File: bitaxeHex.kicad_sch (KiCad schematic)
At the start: 26 parts, among them J1 Screw Terminal, J2 Screw Terminal

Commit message: adjust new mounting hole locations
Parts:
- H10, H13, H14, H15, H5, H6, H7, H8, H9: footprint bitaxe:2.2mm_mounting -> bitaxe:3.1mm_mounting
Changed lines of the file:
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@@
       (effects (font (size 1.27 1.27)) (justify left))
     )
-    (property "Footprint" "bitaxe:2.2mm_mounting" (at 119.38 147.955 0)
+    (property "Footprint" "bitaxe:3.1mm_mounting" (at 119.38 147.955 0)
       (effects (font (size 1.27 1.27)) hide)
     )
@@
       (effects (font (size 1.27 1.27)) (justify left))
     )
-    (property "Footprint" "bitaxe:2.2mm_mounting" (at 119.38 193.675 0)
+    (property "Footprint" "bitaxe:3.1mm_mounting" (at 119.38 193.675 0)
       (effects (font (size 1.27 1.27)) hide)
     )
@@
       (effects (font (size 1.27 1.27)) (justify left))
     )
-    (property "Footprint" "bitaxe:2.2mm_mounting" (at 119.38 180.34 0)
+    (property "Footprint" "bitaxe:3.1mm_mounting" (at 119.38 180.34 0)
       (effects (font (size 1.27 1.27)) hide)
     )
@@
       (effects (font (size 1.27 1.27)) (justify left))
     )
-    (property "Footprint" "bitaxe:2.2mm_mounting" (at 119.38 154.305 0)
+    (property "Footprint" "bitaxe:3.1mm_mounting" (at 119.38 154.305 0)
       (effects (font (size 1.27 1.27)) hide)
     )
@@
       (effects (font (size 1.27 1.27)) (justify left))
     )
-    (property "Footprint" "bitaxe:2.2mm_mounting" (at 119.38 141.605 0)
+    (property "Footprint" "bitaxe:3.1mm_mounting" (at 119.38 141.605 0)
       (effects (font (size 1.27 1.27)) hide)
     )
@@
       (effects (font (size 1.27 1.27)) (justify left))
     )
-    (property "Footprint" "bitaxe:2.2mm_mounting" (at 119.38 160.655 0)
+    (property "Footprint" "bitaxe:3.1mm_mounting" (at 119.38 160.655 0)
       (effects (font (size 1.27 1.27)) hide)
     )
@@
       (effects (font (size 1.27 1.27)) (justify left))
     )
-    (property "Footprint" "bitaxe:2.2mm_mounting" (at 119.38 187.325 0)
+    (property "Footprint" "bitaxe:3.1mm_mounting" (at 119.38 187.325 0)
       (effects (font (size 1.27 1.27)) hide)
     )
@@
       (effects (font (size 1.27 1.27)) (justify left))
     )
-    (property "Footprint" "bitaxe:2.2mm_mounting" (at 119.38 173.99 0)
+    (property "Footprint" "bitaxe:3.1mm_mounting" (at 119.38 173.99 0)
       (effects (font (size 1.27 1.27)) hide)
     )
@@
       (effects (font (size 1.27 1.27)) (justify left))
     )
-    (property "Footprint" "bitaxe:2.2mm_mounting" (at 119.38 167.64 0)
-      (effects (font (size 1.27 1.27)) hide)
-    )
+    (property "Footprint" "bitaxe:3.1mm_mounting" (at 119.38 167.64 0)
+      (effects (font (size 1.27 1.27)) hide)
+    )

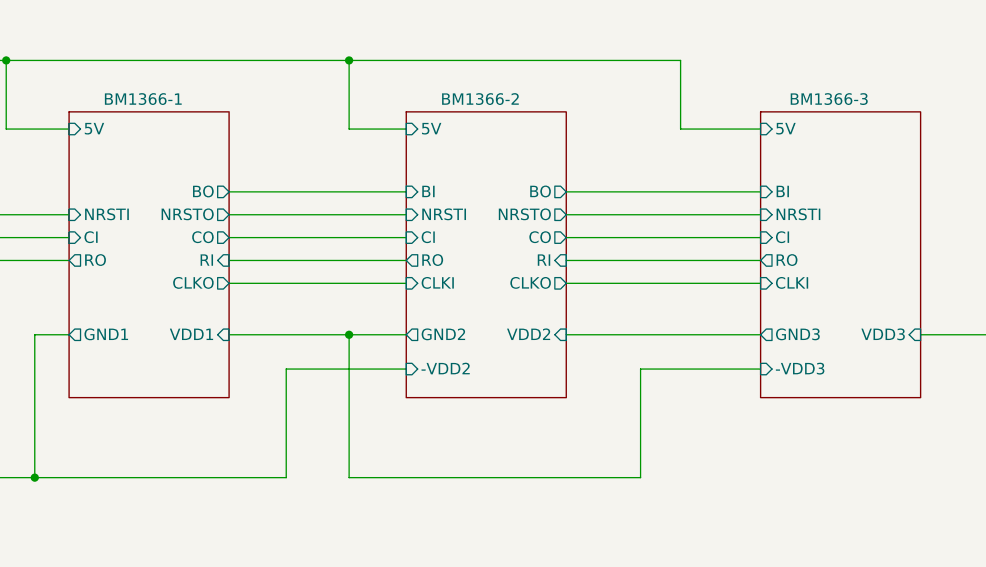
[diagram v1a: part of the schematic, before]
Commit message: remove 33R series resistors and other components, add mounting holes
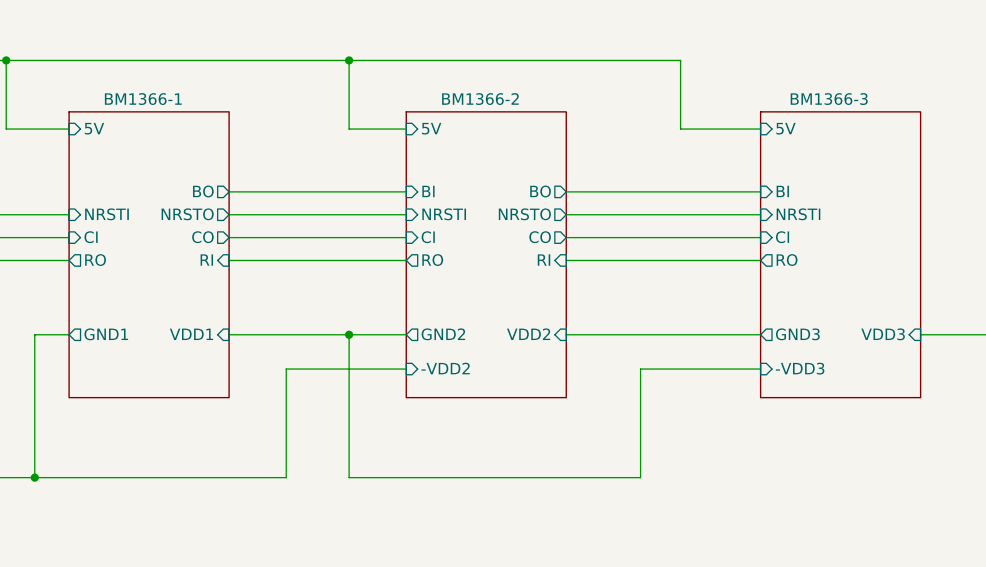
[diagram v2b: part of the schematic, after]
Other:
- sheet BM1366-1 ports: added none; removed CLKO
- sheet BM1366-2 ports: added none; removed CLKI, CLKO
- sheet BM1366-3 ports: added none; removed CLKI
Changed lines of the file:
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@@
   (title_block
     (title "bitaxeHex")
-    (date "2023-12-28")
-    (rev "302")
+    (date "2024-03-09")
+    (rev "303")
   )
   (junction (at 90.805 80.01) (diameter 0) (color 0 0 0 0)
@@
     (stroke (width 0) (type default))
   )
-  (wire (pts (xy 141.605 93.345) (xy 161.29 93.345))
-    (stroke (width 0) (type default))
-  )
   (wire (pts (xy 87.63 95.25) (xy 81.28 95.25))
     (stroke (width 0) (type default))
@@
   )
   (wire (pts (xy 37.465 40.64) (xy 45.72 40.64))
-    (stroke (width 0) (type default))
-  )
-  (wire (pts (xy 179.07 93.345) (xy 200.66 93.345))
     (stroke (width 0) (type default))
   )
@@
       (effects (font (size 1.27 1.27)) (justify right))
     )
-    (pin "CLKO" output (at 141.605 93.345 0)
-      (effects (font (size 1.27 1.27)) (justify right))
-    )
     (pin "CI" input (at 123.825 88.265 180)
       (effects (font (size 1.27 1.27)) (justify left))
@@
       (effects (font (size 1.27 1.27)) (justify left))
     )
-    (pin "CLKI" input (at 161.29 93.345 180)
-      (effects (font (size 1.27 1.27)) (justify left))
-    )
     (pin "CI" input (at 161.29 88.265 180)
       (effects (font (size 1.27 1.27)) (justify left))
@@
     )
     (pin "VDD2" input (at 179.07 99.06 0)
-      (effects (font (size 1.27 1.27)) (justify right))
-    )
-    (pin "CLKO" output (at 179.07 93.345 0)
       (effects (font (size 1.27 1.27)) (justify right))
     )
@@
       (effects (font (size 1.27 1.27)) (justify left))
     )
-    (pin "CLKI" input (at 200.66 93.345 180)
-      (effects (font (size 1.27 1.27)) (justify left))
-    )

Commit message: generate BOM and gerber files for v303
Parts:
- H1, H2, H3, H4: now left out of the parts list
- renumbered H8 to H10, H9 to H11, H10 to H12, H11 to H5, H12 to H6, H5 to H7, H6 to H8, H7 to H9
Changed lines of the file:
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@@
 		(unit 1)
 		(exclude_from_sim no)
-		(in_bom yes)
+		(in_bom no)
 		(on_board yes)
 		(dnp no)
@@
 		(unit 1)
 		(exclude_from_sim no)
-		(in_bom yes)
+		(in_bom no)
 		(on_board yes)
 		(dnp no)
@@
 		(unit 1)
 		(exclude_from_sim no)
-		(in_bom yes)
+		(in_bom no)
 		(on_board yes)
 		(dnp no)
@@
 		(unit 1)
 		(exclude_from_sim no)
-		(in_bom yes)
+		(in_bom no)
 		(on_board yes)
 		(dnp no)
@@
 		(dnp no)
 		(fields_autoplaced yes)
-		(property "Reference" "H6"
+		(property "Reference" "H8"
 			(at 121.92 146.6849 0)
 			(effects
@@
 			(project "bitaxeHex"
 				(path "/e63e39d7-6ac0-4ffd-8aa3-1841a4541b55"
-					(reference "H6")
+					(reference "H8")
 					(unit 1)
 				)
@@
 		(dnp no)
 		(fields_autoplaced yes)
-		(property "Reference" "H11"
+		(property "Reference" "H5"
 			(at 88.265 180.34 90)
 			(effects
@@
 			(project "bitaxeHex"
 				(path "/e63e39d7-6ac0-4ffd-8aa3-1841a4541b55"
-					(reference "H11")
+					(reference "H5")
 					(unit 1)
 				)
@@
 		(dnp no)
 		(fields_autoplaced yes)
-		(property "Reference" "H12"
+		(property "Reference" "H6"
 			(at 88.265 187.325 90)
 			(effects
@@
 			(project "bitaxeHex"
 				(path "/e63e39d7-6ac0-4ffd-8aa3-1841a4541b55"
-					(reference "H12")
+					(reference "H6")
 					(unit 1)
 				)
@@
 		(dnp no)
 		(fields_autoplaced yes)
-		(property "Reference" "H7"
+		(property "Reference" "H9"
 			(at 121.92 153.0349 0)
 			(effects
@@
 			(project "bitaxeHex"
 				(path "/e63e39d7-6ac0-4ffd-8aa3-1841a4541b55"
-					(reference "H7")
+					(reference "H9")
 					(unit 1)
 				)
@@
 		(dnp no)
 		(fields_autoplaced yes)
-		(property "Reference" "H5"
+		(property "Reference" "H7"
 			(at 121.92 140.3349 0)
 			(effects
@@
 			(project "bitaxeHex"
 				(path "/e63e39d7-6ac0-4ffd-8aa3-1841a4541b55"
-					(reference "H5")
+					(reference "H7")
 					(unit 1)
 				)
@@
 		(dnp no)
 		(fields_autoplaced yes)
-		(property "Reference" "H8"
+		(property "Reference" "H10"
 			(at 121.92 159.3849 0)
 			(effects
@@
 			(project "bitaxeHex"
 				(path "/e63e39d7-6ac0-4ffd-8aa3-1841a4541b55"
-					(reference "H8")
+					(reference "H10")
 					(unit 1)
 				)
@@
 		(dnp no)
 		(fields_autoplaced yes)
-		(property "Reference" "H10"
+		(property "Reference" "H12"
 			(at 121.92 172.7199 0)
 			(effects
@@
 			(project "bitaxeHex"
 				(path "/e63e39d7-6ac0-4ffd-8aa3-1841a4541b55"
-					(reference "H10")
+					(reference "H12")
 					(unit 1)
 				)
@@
 		(dnp no)
 		(fields_autoplaced yes)
-		(property "Reference" "H9"
+		(property "Reference" "H11"
 			(at 121.92 166.3699 0)
 			(effects
@@
 			(project "bitaxeHex"
 				(path "/e63e39d7-6ac0-4ffd-8aa3-1841a4541b55"
-					(reference "H9")
-					(unit 1)
-				)
+					(reference "H11")
+					(unit 1)
+				)

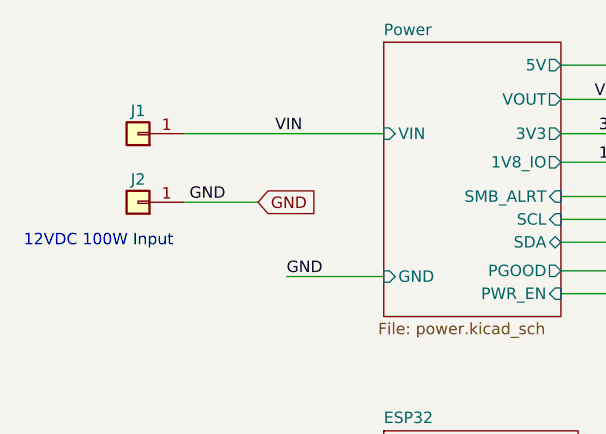
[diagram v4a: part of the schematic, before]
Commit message: swap out electrolytic output capacitor, add XT30 power connector
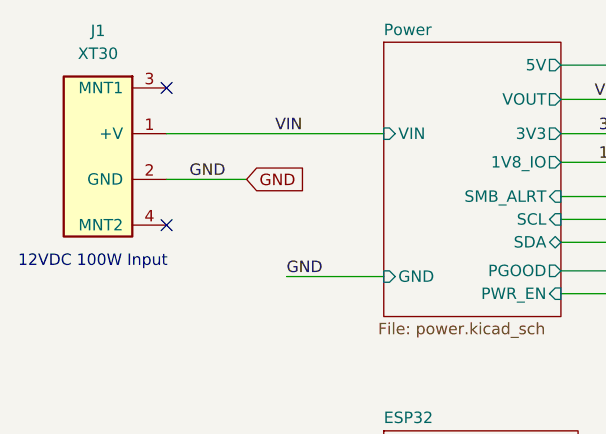
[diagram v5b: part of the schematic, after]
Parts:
- removed J1, J2: Screw Terminal, bitaxe:7771-screw-terminal, symbol Connector_Generic:Conn_01x01
- added J1: XT30, bitaxe:XT30PW-M, symbol bitaxe:XT30PW-M
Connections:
- net GND: now also J1.2 (GND)
- net VIN: now also J1.1 (+V)
- no-connect marks 0 -> 2
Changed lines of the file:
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@@
 		(title "bitaxeHex")
 		(date "2024-03-09")
-		(rev "303")
+		(rev "304")
 	)
 	(junction
@@
 		(color 0 0 0 0)
 	)
+	(no_connect
+		(at 35.56 43.18)
+	)
+	(no_connect
+		(at 35.56 27.94)
+	)
 	(wire
 		(pts
@@
 	(wire
 		(pts
+			(xy 35.56 33.02) (xy 59.69 33.02)
+		)
+		(stroke
+			(width 0)
+			(type default)
+		)
+	)
+	(wire
+		(pts
 			(xy 218.44 99.06) (xy 230.505 99.06)
 		)
@@
 	(wire
 		(pts
+			(xy 35.56 38.1) (xy 44.45 38.1)
+		)
+		(stroke
+			(width 0)
+			(type default)
+		)
+	)
+	(wire
+		(pts
 			(xy 79.375 48.26) (xy 88.265 48.26)
 		)
@@
 	(wire
 		(pts
-			(xy 37.465 40.64) (xy 45.72 40.64)
-		)
-		(stroke
-			(width 0)
-			(type default)
-		)
-	)
-	(wire
-		(pts
 			(xy 81.28 68.58) (xy 85.725 68.58)
 		)
@@
 		(pts
 			(xy 80.645 113.03) (xy 93.345 113.03)
-		)
-		(stroke
-			(width 0)
-			(type default)
-		)
-	)
-	(wire
-		(pts
-			(xy 37.465 33.02) (xy 59.69 33.02)
 		)
 		(stroke
@@
 	(text "12VDC 100W Input"
 		(exclude_from_sim no)
-		(at 19.685 45.72 0)
+		(at 19.05 48.006 0)
 		(effects
 			(font
@@
 	)
 	(label "GND"
-		(at 38.1 40.64 0)
+		(at 38.1 38.1 0)
 		(fields_autoplaced yes)
 		(effects
@@
 	(global_label "GND"
 		(shape input)
-		(at 45.72 40.64 0)
+		(at 44.45 38.1 0)
 		(fields_autoplaced yes)
 		(effects
@@
 		)
 		(property "Intersheetrefs" "${INTERSHEET_REFS}"
-			(at 52.0036 40.5606 0)
-			(effects
-				(font
-					(size 1.27 1.27)
-				)
-				(justify left)
-				(hide yes)
-			)
-		)
-	)
-	(symbol
-		(lib_id "Connector_Generic:Conn_01x01")
-		(at 32.385 33.02 180)
-		(unit 1)
-		(exclude_from_sim no)
-		(in_bom yes)
-		(on_board yes)
-		(dnp no)
-		(property "Reference" "J1"
-			(at 32.385 30.48 0)
-			(effects
-				(font
-					(size 1.27 1.27)
-				)
-			)
-		)
-		(property "Value" "Screw Terminal"
-			(at 32.385 29.21 0)
-			(effects
-				(font
-					(size 1.27 1.27)
-				)
-				(hide yes)
-			)
-		)
-		(property "Footprint" "bitaxe:7771-screw-terminal"
-			(at 32.385 33.02 0)
-			(effects
-				(font
-					(size 1.27 1.27)
-				)
-				(hide yes)
-			)
-		)
-		(property "Datasheet" "https://mm.digikey.com/Volume0/opasdata/d220001/medias/docus/581/Metric_PCB_Screw_Terminals.pdf"
-			(at 32.385 33.02 0)
-			(effects
-				(font
-					(size 1.27 1.27)
-				)
-				(hide yes)
-			)
-		)
-		(property "Description" ""
-			(at 32.385 33.02 0)
-			(effects
-				(font
-					(size 1.27 1.27)
-				)
-				(hide yes)
-			)
-		)
-		(property "DK" "36-7771-ND"
-			(at 32.385 33.02 0)
-			(effects
-				(font
-					(size 1.27 1.27)
-				)
-				(hide yes)
-			)
-		)
-		(property "PARTNO" "36-7771"
-			(at 32.385 33.02 0)
-			(effects
-				(font
-					(size 1.27 1.27)
-				)
-				(hide yes)
-			)
-		)
-		(pin "1"
-		)
-		(instances
-			(project "bitaxeHex"
-				(path "/e63e39d7-6ac0-4ffd-8aa3-1841a4541b55"
-					(reference "J1")
-					(unit 1)
-				)
+			(at 50.7336 38.0206 0)
+			(effects
+				(font
+					(size 1.27 1.27)
+				)
+				(justify left)
+				(hide yes)
 			)
 		)
@@
 	)
 	(symbol
+		(lib_id "bitaxe:XT30PW-M")
+		(at 27.94 35.56 0)
+		(mirror y)
+		(unit 1)
+		(exclude_from_sim no)
+		(in_bom yes)
+		(on_board yes)
+		(dnp no)
+		(fields_autoplaced yes)
+		(property "Reference" "J1"
+			(at 27.94 21.59 0)
+			(effects
+				(font
+					(size 1.27 1.27)
+				)
+			)
+		)
+		(property "Value" "XT30"
+			(at 27.94 24.13 0)
+			(effects
+				(font
+					(size 1.27 1.27)
+				)
+			)
+		)
+		(property "Footprint" "bitaxe:XT30PW-M"
+			(at 27.686 51.308 0)
+			(effects
+				(font
+					(size 1.27 1.27)
+				)
+				(hide yes)
+			)
+		)
+		(property "Datasheet" "~"
+			(at 22.352 40.64 0)
+			(effects
+				(font
+					(size 1.27 1.27)
+				)
+				(hide yes)
+			)
+		)
+		(property "Description" ""
+			(at 27.94 35.56 0)
+			(effects
+				(font
+					(size 1.27 1.27)
+				)
+				(hide yes)
+			)
+		)
+		(property "PARTNO" "XT30PW-M"
+			(at 27.686 49.022 0)
+			(effects
+				(font
+					(size 1.27 1.27)
+				)
+				(hide yes)
+			)
+		)
+		(property "DK" "~"
+			(at 22.352 42.672 0)
+			(effects
+				(font
+					(size 1.27 1.27)
+				)
+				(hide yes)
+			)
+		)
+		(pin "3"
+		)
+		(pin "4"
+		)
+		(pin "1"
+		)
+		(pin "2"
+		)
+		(instances
+			(project "bitaxeHex"
+				(path "/e63e39d7-6ac0-4ffd-8aa3-1841a4541b55"
+					(reference "J1")
+					(unit 1)
+				)
+			)
+		)
+	)
+	(symbol
 		(lib_id "Mechanical:MountingHole_Pad")
 		(at 84.455 153.67 270)
@@
 					(unit 1)
 				)
-			)
-		)
-	)
-	(symbol
-		(lib_id "Connector_Generic:Conn_01x01")
-		(at 32.385 40.64 180)
-		(unit 1)
-		(exclude_from_sim no)
-		(in_bom yes)
-		(on_board yes)
-		(dnp no)
-		(property "Reference" "J2"
-			(at 32.385 38.1 0)
-			(effects
-				(font
-					(size 1.27 1.27)
-				)
-			)
-		)
-		(property "Value" "Screw Terminal"
-			(at 32.385 36.83 0)
-			(effects
-				(font
-					(size 1.27 1.27)
-				)
-				(hide yes)
-			)
-		)
-		(property "Footprint" "bitaxe:7771-screw-terminal"
-			(at 32.385 40.64 0)
-			(effects
-				(font
-					(size 1.27 1.27)
-				)
-				(hide yes)
-			)
-		)
-		(property "Datasheet" "https://mm.digikey.com/Volume0/opasdata/d220001/medias/docus/581/Metric_PCB_Screw_Terminals.pdf"
-			(at 32.385 40.64 0)
-			(effects
-				(font
-					(size 1.27 1.27)
-				)
-				(hide yes)
-			)
-		)
-		(property "Description" ""
-			(at 32.385 40.64 0)
-			(effects
-				(font
-					(size 1.27 1.27)
-				)
-				(hide yes)
-			)
-		)
-		(property "DK" "36-7771-ND"
-			(at 32.385 40.64 0)
-			(effects
-				(font
-					(size 1.27 1.27)
-				)
-				(hide yes)
-			)
-		)
-		(property "PARTNO" "36-7771"
-			(at 32.385 40.64 0)
-			(effects
-				(font
-					(size 1.27 1.27)
-				)
-				(hide yes)
-			)
-		)
-		(pin "1"
-		)
-		(instances
-			(project "bitaxeHex"
-				(path "/e63e39d7-6ac0-4ffd-8aa3-1841a4541b55"
-					(reference "J2")
-					(unit 1)
-				)
